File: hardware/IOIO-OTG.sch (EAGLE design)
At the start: 60 parts, among them Q1 IRLML2244, Q2 2N7002PW, Q3 AO3404A, U1 PIC24FJ256GB206, U2 TPS62133RGTT, U3 VREG_MIC5216

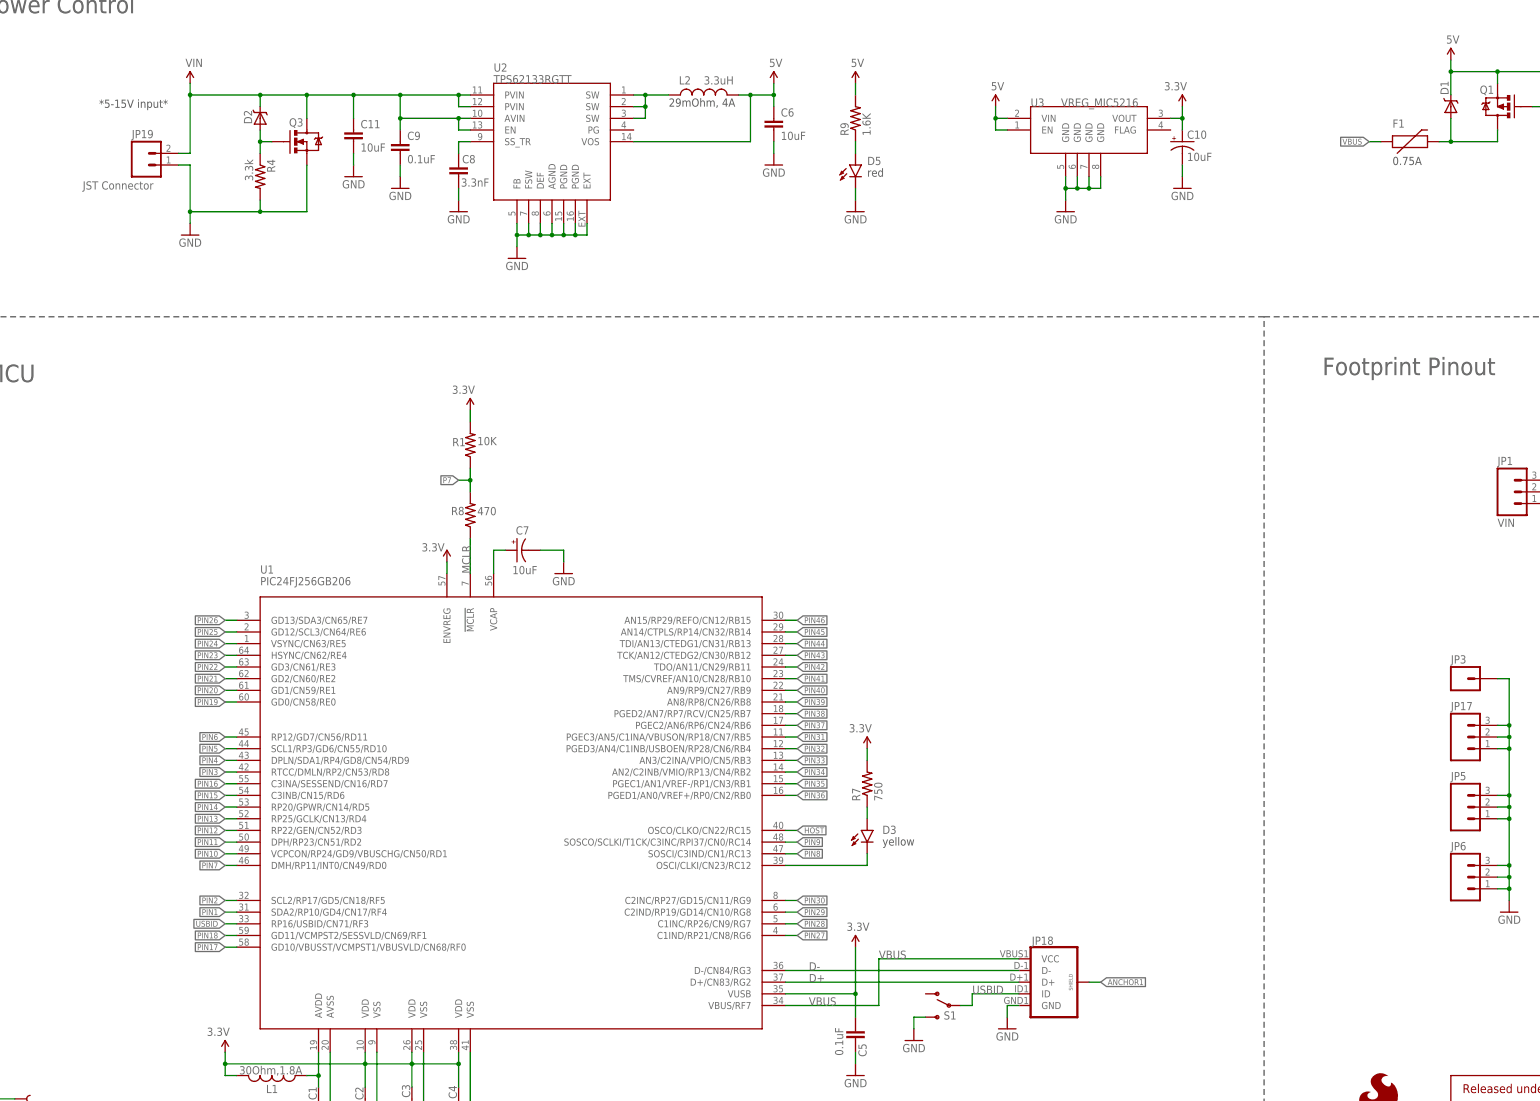
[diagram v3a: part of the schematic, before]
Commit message: swapping out devices to include PROD_IDs
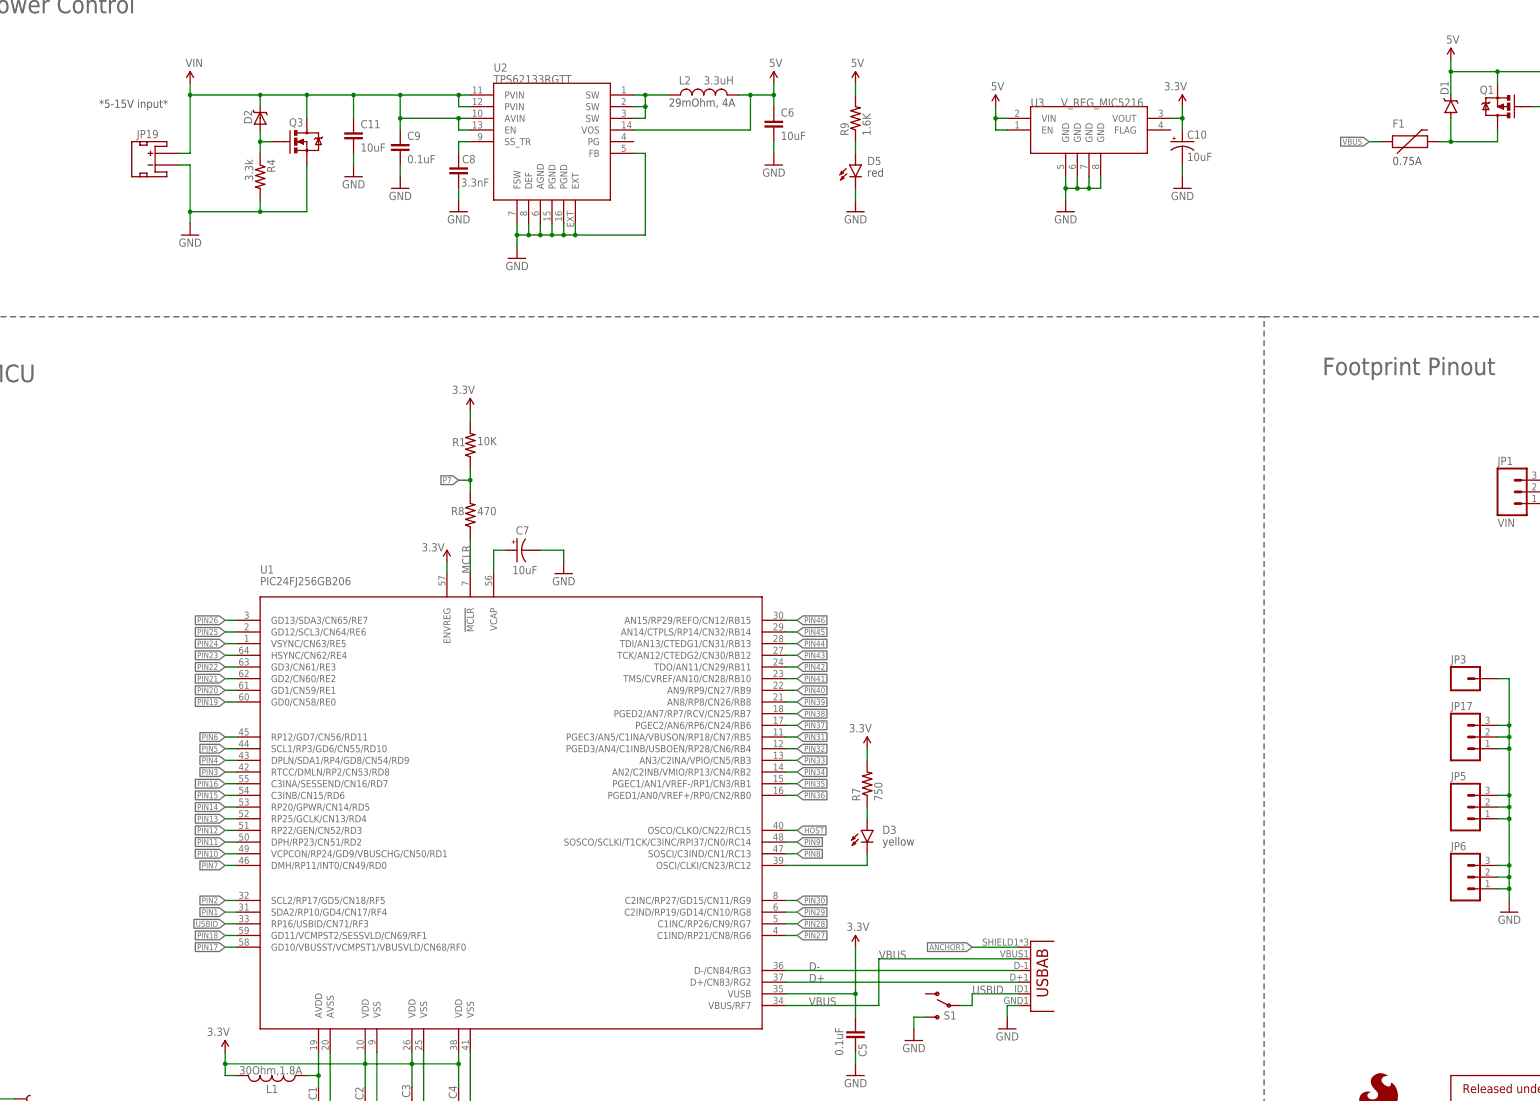
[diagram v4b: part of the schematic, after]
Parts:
- removed JP18: (no value), SparkFun-Connectors:USB_MICROB_PLUGCONN-11752
- added U4: (no value), SparkFun-Connectors:USB-ABCONN-11794
- C10: device SparkFun-Passives:CAP_POL1206 -> SparkFun-Capacitors:10UF-16V-10%(TANT)
- C6: device SparkFun-Passives:CAP0805 -> SparkFun-Capacitors:10UF10V10%(0805)
- C7: device SparkFun:CAP_POL1206 -> SparkFun-Capacitors:10UF-16V-10%(TANT)
- D1: device SparkFun-DiscreteSemi:DIODE-SCHOTTKY_ -> SparkFun-DiscreteSemi:DIODE-SCHOTTKY-B340A
- JP19: value JST Connector -> JST; device SparkFun:M02-JST-2MM-SMT -> SparkFun-Connectors:JST_2MM_MALE
- U2: device SparkFun-PowerIC:TPS6214X -> SparkFun-PowerIC:TPS62133RGTT""
- U3: value VREG_MIC5216 -> V_REG_MIC5216; device SparkFun-PowerIC:VREG_MIC5216 -> SparkFun-PowerIC:V_REG_MIC5216
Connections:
- net ANCHOR1: now also U4.SHIELD; no longer JP18.SHIELD
- net D+: now also U4.D+; no longer JP18.D+
- net D-: now also U4.D-; no longer JP18.D-
- net GND: now also JP19.-, U4.GND; no longer JP18.GND, JP19.1
- net USBID: now also U4.USBID; no longer JP18.ID
- net VBUS: now also U4.VBUS; no longer JP18.VCC
- net VIN: now also JP19.+; no longer JP19.2
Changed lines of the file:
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@@
 <part name="C3" library="SparkFun-Capacitors" deviceset="0.1UF-25V(+80/-20%)(0603)" device="" value="0.1uF"/>
 <part name="C4" library="SparkFun-Capacitors" deviceset="0.1UF-25V(+80/-20%)(0603)" device="" value="0.1uF"/>
-<part name="C7" library="SparkFun" deviceset="CAP_POL" device="1206" value="10uF"/>
+<part name="C7" library="SparkFun-Capacitors" deviceset="10UF-16V-10%(TANT)" device="" value="10uF"/>
 <part name="P+1" library="SparkFun" deviceset="3.3V" device=""/>
 <part name="P+2" library="SparkFun" deviceset="3.3V" device=""/>
@@
 <part name="JP17" library="SparkFun" deviceset="M03" device="PTH"/>
 <part name="U$10" library="SparkFun" deviceset="5V" device=""/>
-<part name="JP19" library="SparkFun" deviceset="M02" device="-JST-2MM-SMT" value="JST Connector"/>
 <part name="GND17" library="SparkFun" deviceset="GND" device=""/>
-<part name="U2" library="SparkFun-PowerIC" deviceset="TPS6214X" device="" value="TPS62133RGTT"/>
+<part name="U2" library="SparkFun-PowerIC" deviceset="TPS62133RGTT" device="&quot;&quot;" value="TPS62133RGTT"/>
 <part name="Q1" library="SparkFun-DiscreteSemi" deviceset="MOSFET-PCHANNEL" device="SMD" value="IRLML2244"/>
 <part name="Q2" library="SparkFun-DiscreteSemi" deviceset="MOSFET-NCHANNEL" device="SOT323" value="2N7002PW">
 <attribute name="PART#" value="2N7002PW"/>
 </part>
-<part name="D1" library="SparkFun-DiscreteSemi" deviceset="DIODE-SCHOTTKY" device="_" value="B340A">
+<part name="D1" library="SparkFun-DiscreteSemi" deviceset="DIODE-SCHOTTKY" device="-B340A" value="B340A">
 <attribute name="PART#" value="B340A"/>
 </part>
@@
 </part>
 <part name="R2" library="SparkFun-Resistors" deviceset="100KOHM-1/10W-1%(0603)" device="" value="100k"/>
-<part name="C10" library="SparkFun-Passives" deviceset="CAP_POL" device="1206" value="10uF">
+<part name="C10" library="SparkFun-Capacitors" deviceset="10UF-16V-10%(TANT)" device="" value="10uF">
 <attribute name="PART#" value="TAJA106K016RNJ"/>
 </part>
-<part name="C6" library="SparkFun-Passives" deviceset="CAP" device="0805" value="10uF">
+<part name="C6" library="SparkFun-Capacitors" deviceset="10UF10V10%(0805)" device="" value="10uF">
 <attribute name="PART#" value="LMK212BJ106KG-T"/>
 </part>
@@
 </part>
 <part name="U$8" library="SparkFun-Aesthetics" deviceset="VIN" device=""/>
-<part name="U3" library="SparkFun-PowerIC" deviceset="VREG_MIC5216" device=""/>
+<part name="U3" library="SparkFun-PowerIC" deviceset="V_REG_MIC5216" device=""/>
 <part name="U$7" library="SparkFun" deviceset="5V" device=""/>
 <part name="GND8" library="SparkFun" deviceset="GND" device=""/>
@@
 <part name="C9" library="SparkFun-Capacitors" deviceset="0.1UF-25V(+80/-20%)(0603)" device="" value="0.1uF"/>
 <part name="GND20" library="SparkFun" deviceset="GND" device=""/>
-<part name="JP18" library="SparkFun-Connectors" deviceset="USB_MICROB_PLUG" device="CONN-11752"/>
 <part name="LOGO1" library="SparkFun-Aesthetics" deviceset="OSHW-LOGO" device="S" value="OSHW-LOGOS"/>
 <part name="FRAME2" library="SparkFun-Aesthetics" deviceset="FRAME-LEDGER" device=""/>
 <part name="LOGO2" library="SparkFun-Aesthetics" deviceset="SFE_LOGO_FLAME" device=".1_INCH"/>
 <part name="LOGO4" library="SparkFun-Aesthetics" deviceset="SFE_LOGO_NAME_FLAME" device=".1_INCH"/>
+<part name="U4" library="SparkFun-Connectors" deviceset="USB-AB" device="CONN-11794"/>
+<part name="JP19" library="SparkFun-Connectors" deviceset="JST_2MM_MALE" device="" value="JST"/>
 </parts>
 <sheets>
@@
 </instance>
 <instance part="U$10" gate="G$1" x="182.88" y="251.46"/>
-<instance part="JP19" gate="G$1" x="45.72" y="233.68" smashed="yes">
-<attribute name="VALUE" x="32.512" y="228.346" size="1.778" layer="96"/>
-<attribute name="NAME" x="43.18" y="239.522" size="1.778" layer="95"/>
-</instance>
 <instance part="GND17" gate="1" x="55.88" y="218.44" rot="MR0"/>
 <instance part="U2" gate="G$1" x="134.62" y="241.3"/>
@@
 <instance part="C9" gate="G$1" x="101.6" y="236.22"/>
 <instance part="GND20" gate="1" x="101.6" y="228.6" rot="MR0"/>
-<instance part="JP18" gate="G$1" x="243.84" y="55.88"/>
 <instance part="LOGO1" gate="G$1" x="314.96" y="12.7"/>
 <instance part="FRAME2" gate="G$1" x="0" y="0"/>
@@
 <instance part="LOGO2" gate="G$1" x="309.88" y="22.86"/>
 <instance part="LOGO4" gate="G$1" x="231.14" y="0"/>
+<instance part="U4" gate="G$1" x="241.3" y="55.88" rot="MR180"/>
+<instance part="JP19" gate="G$1" x="48.26" y="233.68" smashed="yes" rot="R90">
+<attribute name="NAME" x="49.022" y="241.3" size="1.778" layer="95" rot="R180"/>
+</instance>
 </instances>
 <busses>
@@
 <wire x1="53.34" y1="233.68" x2="55.88" y2="233.68" width="0.1524" layer="91"/>
 <wire x1="55.88" y1="233.68" x2="55.88" y2="223.52" width="0.1524" layer="91"/>
-<pinref part="JP19" gate="G$1" pin="1"/>
 <pinref part="GND17" gate="1" pin="GND"/>
 <wire x1="55.88" y1="223.52" x2="55.88" y2="220.98" width="0.1524" layer="91"/>
@@
 <wire x1="71.12" y1="223.52" x2="55.88" y2="223.52" width="0.1524" layer="91"/>
 <junction x="55.88" y="223.52"/>
+<pinref part="JP19" gate="G$1" pin="-"/>
 </segment>
 <segment>
@@
 <segment>
 <pinref part="U2" gate="G$1" pin="FB"/>
-<wire x1="127" y1="220.98" x2="127" y2="218.44" width="0.1524" layer="91"/>
 <pinref part="U2" gate="G$1" pin="EXT"/>
 <wire x1="127" y1="218.44" x2="129.54" y2="218.44" width="0.1524" layer="91"/>
@@
 <wire x1="134.62" y1="218.44" x2="137.16" y2="218.44" width="0.1524" layer="91"/>
 <wire x1="137.16" y1="218.44" x2="139.7" y2="218.44" width="0.1524" layer="91"/>
-<wire x1="139.7" y1="218.44" x2="142.24" y2="218.44" width="0.1524" layer="91"/>
-<wire x1="142.24" y1="218.44" x2="142.24" y2="220.98" width="0.1524" layer="91"/>
+<wire x1="139.7" y1="218.44" x2="139.7" y2="220.98" width="0.1524" layer="91"/>
 <pinref part="U2" gate="G$1" pin="FSW"/>
+<wire x1="127" y1="220.98" x2="127" y2="218.44" width="0.1524" layer="91"/>
+<junction x="127" y="218.44"/>
+<pinref part="U2" gate="G$1" pin="DEF"/>
 <wire x1="129.54" y1="220.98" x2="129.54" y2="218.44" width="0.1524" layer="91"/>
 <junction x="129.54" y="218.44"/>
-<pinref part="U2" gate="G$1" pin="DEF"/>
+<pinref part="U2" gate="G$1" pin="AGND"/>
 <wire x1="132.08" y1="220.98" x2="132.08" y2="218.44" width="0.1524" layer="91"/>
 <junction x="132.08" y="218.44"/>
-<pinref part="U2" gate="G$1" pin="AGND"/>
+<pinref part="U2" gate="G$1" pin="PGND@15"/>
 <wire x1="134.62" y1="220.98" x2="134.62" y2="218.44" width="0.1524" layer="91"/>
 <junction x="134.62" y="218.44"/>
-<pinref part="U2" gate="G$1" pin="PGND@15"/>
+<pinref part="U2" gate="G$1" pin="PGND@16"/>
 <wire x1="137.16" y1="220.98" x2="137.16" y2="218.44" width="0.1524" layer="91"/>
 <junction x="137.16" y="218.44"/>
-<pinref part="U2" gate="G$1" pin="PGND@16"/>
-<wire x1="139.7" y1="220.98" x2="139.7" y2="218.44" width="0.1524" layer="91"/>
-<junction x="139.7" y="218.44"/>
 <pinref part="GND8" gate="1" pin="GND"/>
 <wire x1="127" y1="215.9" x2="127" y2="218.44" width="0.1524" layer="91"/>
-<junction x="127" y="218.44"/>
+<wire x1="152.4" y1="236.22" x2="154.94" y2="236.22" width="0.1524" layer="91"/>
+<wire x1="154.94" y1="236.22" x2="154.94" y2="218.44" width="0.1524" layer="91"/>
+<wire x1="154.94" y1="218.44" x2="139.7" y2="218.44" width="0.1524" layer="91"/>
+<junction x="139.7" y="218.44"/>
 </segment>
 <segment>
@@
 <wire x1="233.68" y1="50.8" x2="233.68" y2="48.26" width="0.1524" layer="91"/>
 <pinref part="GND18" gate="1" pin="GND"/>
-<pinref part="JP18" gate="G$1" pin="GND"/>
+<pinref part="U4" gate="G$1" pin="GND"/>
 </segment>
 <segment>
@@
 <segment>
 <pinref part="U2" gate="G$1" pin="VOS"/>
-<wire x1="152.4" y1="238.76" x2="177.8" y2="238.76" width="0.1524" layer="91"/>
-<wire x1="177.8" y1="238.76" x2="177.8" y2="248.92" width="0.1524" layer="91"/>
+<wire x1="152.4" y1="241.3" x2="177.8" y2="241.3" width="0.1524" layer="91"/>
+<wire x1="177.8" y1="241.3" x2="177.8" y2="248.92" width="0.1524" layer="91"/>
 <pinref part="L2" gate="G$1" pin="2"/>
 <wire x1="177.8" y1="248.92" x2="175.26" y2="248.92" width="0.1524" layer="91"/>
@@
 <pinref part="U1" gate="G$1" pin="D-/CN84/RG3"/>
 <label x="190.5" y="58.42" size="1.778" layer="95"/>
-<pinref part="JP18" gate="G$1" pin="D-"/>
+<pinref part="U4" gate="G$1" pin="D-"/>
 </segment>
 <segment>
@@
 <pinref part="U1" gate="G$1" pin="D+/CN83/RG2"/>
 <label x="190.5" y="55.88" size="1.778" layer="95"/>
-<pinref part="JP18" gate="G$1" pin="D+"/>
+<pinref part="U4" gate="G$1" pin="D+"/>
 </segment>
 <segment>
@@
 <junction x="81.28" y="248.92"/>
 <wire x1="91.44" y1="248.92" x2="81.28" y2="248.92" width="0.1524" layer="91"/>
-<pinref part="JP19" gate="G$1" pin="2"/>
 <wire x1="53.34" y1="236.22" x2="55.88" y2="236.22" width="0.1524" layer="91"/>
 <wire x1="55.88" y1="236.22" x2="55.88" y2="248.92" width="0.1524" layer="91"/>
@@
 <wire x1="114.3" y1="243.84" x2="101.6" y2="243.84" width="0.1524" layer="91"/>
 <junction x="101.6" y="243.84"/>
+<pinref part="JP19" gate="G$1" pin="+"/>
 </segment>
 </net>
@@
 <pinref part="S1" gate="G$1" pin="P"/>
 <wire x1="226.06" y1="50.8" x2="223.52" y2="50.8" width="0.1524" layer="91"/>
-<pinref part="JP18" gate="G$1" pin="ID"/>
+<pinref part="U4" gate="G$1" pin="USBID"/>
 </segment>
 <segment>
@@
 <label x="205.74" y="60.96" size="1.778" layer="95"/>
 <label x="190.5" y="50.8" size="1.778" layer="95"/>
-<pinref part="JP18" gate="G$1" pin="VCC"/>
+<pinref part="U4" gate="G$1" pin="VBUS"/>
 </segment>
 <segment>
@@
 <net name="ANCHOR1" class="0">
 <segment>
-<pinref part="JP18" gate="G$1" pin="SHIELD"/>
-<wire x1="251.46" y1="55.88" x2="254" y2="55.88" width="0.1524" layer="91"/>
-<label x="254" y="55.88" size="1.27" layer="95" xref="yes"/>
-</segment>
-</net>
+<pinref part="U4" gate="G$1" pin="SHIELD"/>
+<wire x1="236.22" y1="63.5" x2="226.06" y2="63.5" width="0.1524" layer="91"/>
+<label x="226.06" y="63.5" size="1.27" layer="95" rot="R180" xref="yes"/>
+</segment>
+</net>

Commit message: more PROD_IDs
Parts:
- C11: device SparkFun-Passives:CAP1210 -> SparkFun-Capacitors:10UF50V20%(1210)
- L2: device SparkFun-Passives:INDUCTORCR54 -> SparkFun-Passives:INDUCTORCR54-3.3UH
- Q1: device SparkFun-DiscreteSemi:MOSFET-PCHANNELSMD -> SparkFun-DiscreteSemi:MOSFET-PCHANNELIRLML2244
- Q2: device SparkFun-DiscreteSemi:MOSFET-NCHANNELSOT323 -> SparkFun-DiscreteSemi:MOSFET-NCHANNEL2N7002PW
- U1: device SparkFun-DigitalIC:PIC24FXXXDAX06 -> SparkFun-DigitalIC:PIC24FXXXGPX06
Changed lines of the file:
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@@
 </classes>
 <parts>
-<part name="U1" library="SparkFun-DigitalIC" deviceset="PIC24FXXXDAX06" device="" value="PIC24FJ256GB206"/>
+<part name="U1" library="SparkFun-DigitalIC" deviceset="PIC24FXXXGPX06" device="" value="PIC24FJ256GB206"/>
 <part name="C1" library="SparkFun-Capacitors" deviceset="0.1UF-25V(+80/-20%)(0603)" device="" value="0.1uF"/>
 <part name="C2" library="SparkFun-Capacitors" deviceset="0.1UF-25V(+80/-20%)(0603)" device="" value="0.1uF"/>
@@
 <part name="GND17" library="SparkFun" deviceset="GND" device=""/>
 <part name="U2" library="SparkFun-PowerIC" deviceset="TPS62133RGTT" device="&quot;&quot;" value="TPS62133RGTT"/>
-<part name="Q1" library="SparkFun-DiscreteSemi" deviceset="MOSFET-PCHANNEL" device="SMD" value="IRLML2244"/>
-<part name="Q2" library="SparkFun-DiscreteSemi" deviceset="MOSFET-NCHANNEL" device="SOT323" value="2N7002PW">
+<part name="Q1" library="SparkFun-DiscreteSemi" deviceset="MOSFET-PCHANNEL" device="IRLML2244" value="IRLML2244"/>
+<part name="Q2" library="SparkFun-DiscreteSemi" deviceset="MOSFET-NCHANNEL" device="2N7002PW" value="2N7002PW">
 <attribute name="PART#" value="2N7002PW"/>
 </part>
@@
 </part>
 <part name="C8" library="SparkFun-Capacitors" deviceset="3.3NF-100V-10%(0603)" device="" value="3.3nF"/>
-<part name="C11" library="SparkFun-Passives" deviceset="CAP" device="1210" value="10uF">
+<part name="C11" library="SparkFun-Capacitors" deviceset="10UF50V20%(1210)" device="" value="10uF">
 <attribute name="PART#" value="UMK325C7106MM-T"/>
 </part>
-<part name="L2" library="SparkFun-Passives" deviceset="INDUCTOR" device="CR54" value="VLC5045T-3R3N">
+<part name="L2" library="SparkFun-Passives" deviceset="INDUCTOR" device="CR54-3.3UH" value="VLC5045T-3R3N">
 <attribute name="AM" value="3.3uH"/>
 </part>
@@
 </part>
 <part name="L1" library="SparkFun-Passives" deviceset="INDUCTOR" device="30OHM,1.8A" value="30Ohm,1.8A"/>
-<part name="S1" library="SparkFun-Electromechanical" deviceset="SWITCH_SPDT" device="" value=""/>
+<part name="S1" library="SparkFun-Electromechanical" deviceset="SWITCH_SPDT" device="" value="SWITCH_SPDT"/>
 <part name="JP9" library="SparkFun-Connectors" deviceset="M11" device="1X11_NO_SILK" value=""/>
 <part name="JP14" library="SparkFun" deviceset="M01" device="PTH" value=""/>
@@
 <instance part="S1" gate="G$1" x="220.98" y="50.8" smashed="yes" rot="MR0">
 <attribute name="NAME" x="222.631" y="47.752" size="1.778" layer="95" rot="MR0"/>
-<attribute name="VALUE" x="223.52" y="54.61" size="1.778" layer="96" rot="MR0"/>
 </instance>
 <instance part="JP9" gate="G$1" x="355.6" y="71.12"/>
